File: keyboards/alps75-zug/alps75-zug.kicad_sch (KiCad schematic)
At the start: 176 parts, among them SW1 SW_Push, SW10 SW_Push, SW11 SW_Push, SW12 SW_Push, SW13 SW_Push, SW14 SW_Push, SW15 SW_Push, SW16 SW_Push, SW17 SW_Push, SW18 SW_Push, SW19 SW_Push, SW2 SW_Push, SW20 SW_Push, SW21 SW_Push, SW22 SW_Push, SW23 SW_Push, SW24 SW_Push, SW25 SW_Push, SW26 SW_Push, SW27 SW_Push, SW28 SW_Push, SW29 SW_Push, SW3 SW_Push, SW30 SW_Push, SW31 SW_Push, SW32 SW_Push, SW33 SW_Push, SW34 SW_Push, SW35 SW_Push, SW36 SW_Push, SW37 SW_Push, SW38 SW_Push, SW39 SW_Push, SW4 SW_Push, SW40 SW_Push, SW41 SW_Push, SW42 SW_Push, SW43 SW_Push, SW44 SW_Push, SW45 SW_Push, SW46 SW_Push, SW47 SW_Push, SW48 SW_Push, SW49 SW_Push, SW5 SW_Push, SW50 SW_Push, SW51 SW_Push, SW52 SW_Push, SW53 SW_Push, SW54 SW_Push, SW55 SW_Push, SW56 SW_Push, SW57 SW_Push, SW58 SW_Push, SW59 SW_Push, SW6 SW_Push, SW60 SW_Push, SW61 SW_Push, SW62 SW_Push, SW63 SW_Push, SW64 SW_Push, SW65 SW_Push, SW66 SW_Push, SW67 SW_Push, SW68 SW_Push, SW69 SW_Push, SW7 SW_Push, SW70 SW_Push, SW71 SW_Push, SW72 SW_Push, SW73 SW_Push, SW74 SW_Push, SW75 SW_Push, SW76 SW_Push, SW77 SW_Push, SW78 SW_Push, SW79 SW_Push, SW8 SW_Push, SW80 SW_Push, SW81 SW_Push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

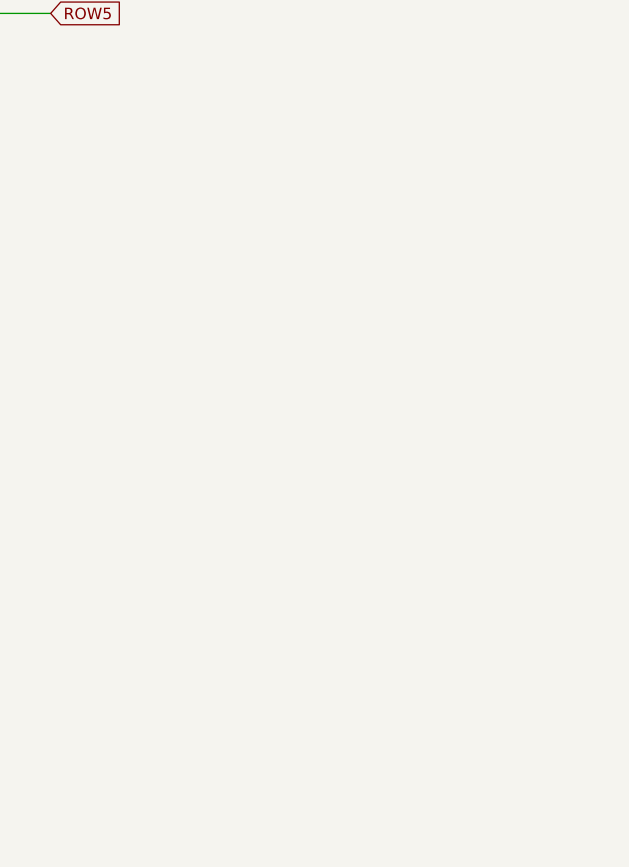
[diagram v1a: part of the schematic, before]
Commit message: Connected all diodes for F-keys + move COL14 wire out of way
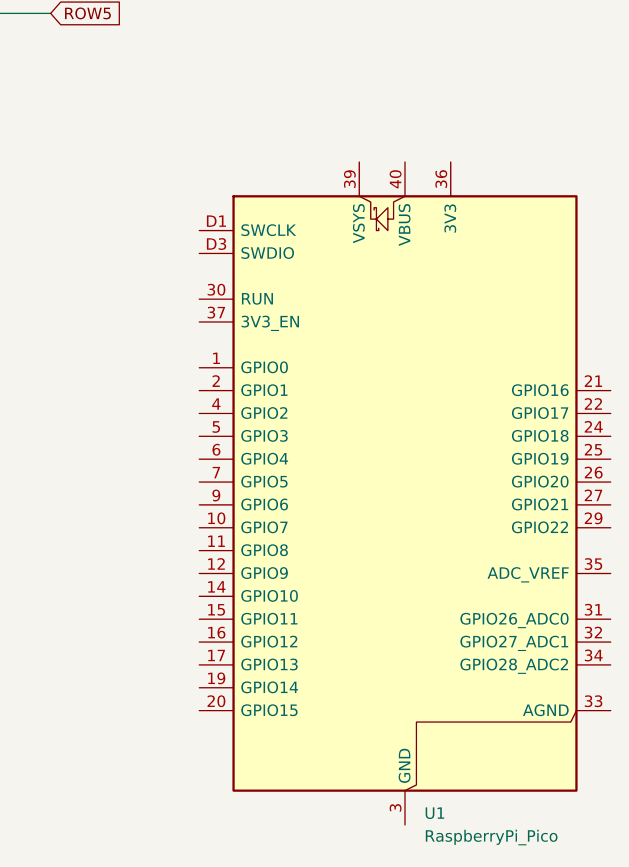
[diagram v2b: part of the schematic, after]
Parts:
- added U1: RaspberryPi_Pico, Module:RaspberryPi_Pico_SMD_HandSolder, symbol MCU_Module:RaspberryPi_Pico_Debug
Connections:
- new net: U1.13 (GND), U1.18 (GND), U1.23 (GND), U1.28 (GND), U1.3 (GND), U1.38 (GND), U1.8 (GND), U1.D2 (GND)
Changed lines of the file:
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@@
+	)
+	(symbol
+		(lib_id "MCU_Module:RaspberryPi_Pico_Debug")
+		(at 280.67 191.77 0)
+		(unit 1)
+		(body_style 1)
+		(exclude_from_sim no)
+		(in_bom yes)
+		(on_board yes)
+		(in_pos_files yes)
+		(dnp no)
+		(fields_autoplaced yes)
+		(property "Reference" "U1"
+			(at 282.8133 226.06 0)
+			(show_name no)
+			(do_not_autoplace no)
+			(effects
+				(font
+					(size 1.27 1.27)
+				)
+				(justify left)
+			)
+		)
+		(property "Value" "RaspberryPi_Pico"
+			(at 282.8133 228.6 0)
+			(show_name no)
+			(do_not_autoplace no)
+			(effects
+				(font
+					(size 1.27 1.27)
+				)
+				(justify left)
+			)
+		)
+		(property "Footprint" "Module:RaspberryPi_Pico_SMD_HandSolder"
+			(at 280.67 238.76 0)
+			(hide yes)
+			(show_name no)
+			(do_not_autoplace no)
+			(effects
+				(font
+					(size 1.27 1.27)
+				)
+			)
+		)
+		(property "Datasheet" "https://datasheets.raspberrypi.com/pico/pico-datasheet.pdf"
+			(at 280.67 241.3 0)
+			(hide yes)
+			(show_name no)
+			(do_not_autoplace no)
+			(effects
+				(font
+					(size 1.27 1.27)
+				)
+			)
+		)
+		(property "Description" "Versatile and inexpensive microcontroller module (with debug pins) powered by RP2040 dual-core Arm Cortex-M0+ processor up to 133 MHz, 264kB SRAM, 2MB QSPI flash; also supports Raspberry Pi Pico 2"
+			(at 280.67 243.84 0)
+			(hide yes)
+			(show_name no)
+			(do_not_autoplace no)
+			(effects
+				(font
+					(size 1.27 1.27)
+				)
+			)
+		)
+		(pin "25"
+		)
+		(pin "26"
+		)
+		(pin "24"
+		)
+		(pin "27"
+		)
+		(pin "22"
+		)
+		(pin "23"
+		)
+		(pin "5"
+		)
+		(pin "21"
+		)
+		(pin "20"
+		)
+		(pin "19"
+		)
+		(pin "18"
+		)
+		(pin "17"
+		)
+		(pin "16"
+		)
+		(pin "15"
+		)
+		(pin "14"
+		)
+		(pin "13"
+		)
+		(pin "12"
+		)
+		(pin "11"
+		)
+		(pin "9"
+		)
+		(pin "10"
+		)
+		(pin "7"
+		)
+		(pin "8"
+		)
+		(pin "6"
+		)
+		(pin "1"
+		)
+		(pin "2"
+		)
+		(pin "3"
+		)
+		(pin "4"
+		)
+		(pin "D3"
+		)
+		(pin "29"
+		)
+		(pin "30"
+		)
+		(pin "31"
+		)
+		(pin "32"
+		)
+		(pin "33"
+		)
+		(pin "34"
+		)
+		(pin "35"
+		)
+		(pin "28"
+		)
+		(pin "36"
+		)
+		(pin "D2"
+		)
+		(pin "D1"
+		)
+		(pin "40"
+		)
+		(pin "39"
+		)
+		(pin "38"
+		)
+		(pin "37"
+		)
+		(instances
+			(project "alps75-zug"
+				(path "/52ee5249-2c64-4583-bfc6-5b6d91f4f70c"
+					(reference "U1")
+					(unit 1)
+				)
+			)
+		)
 	)
 	(symbol

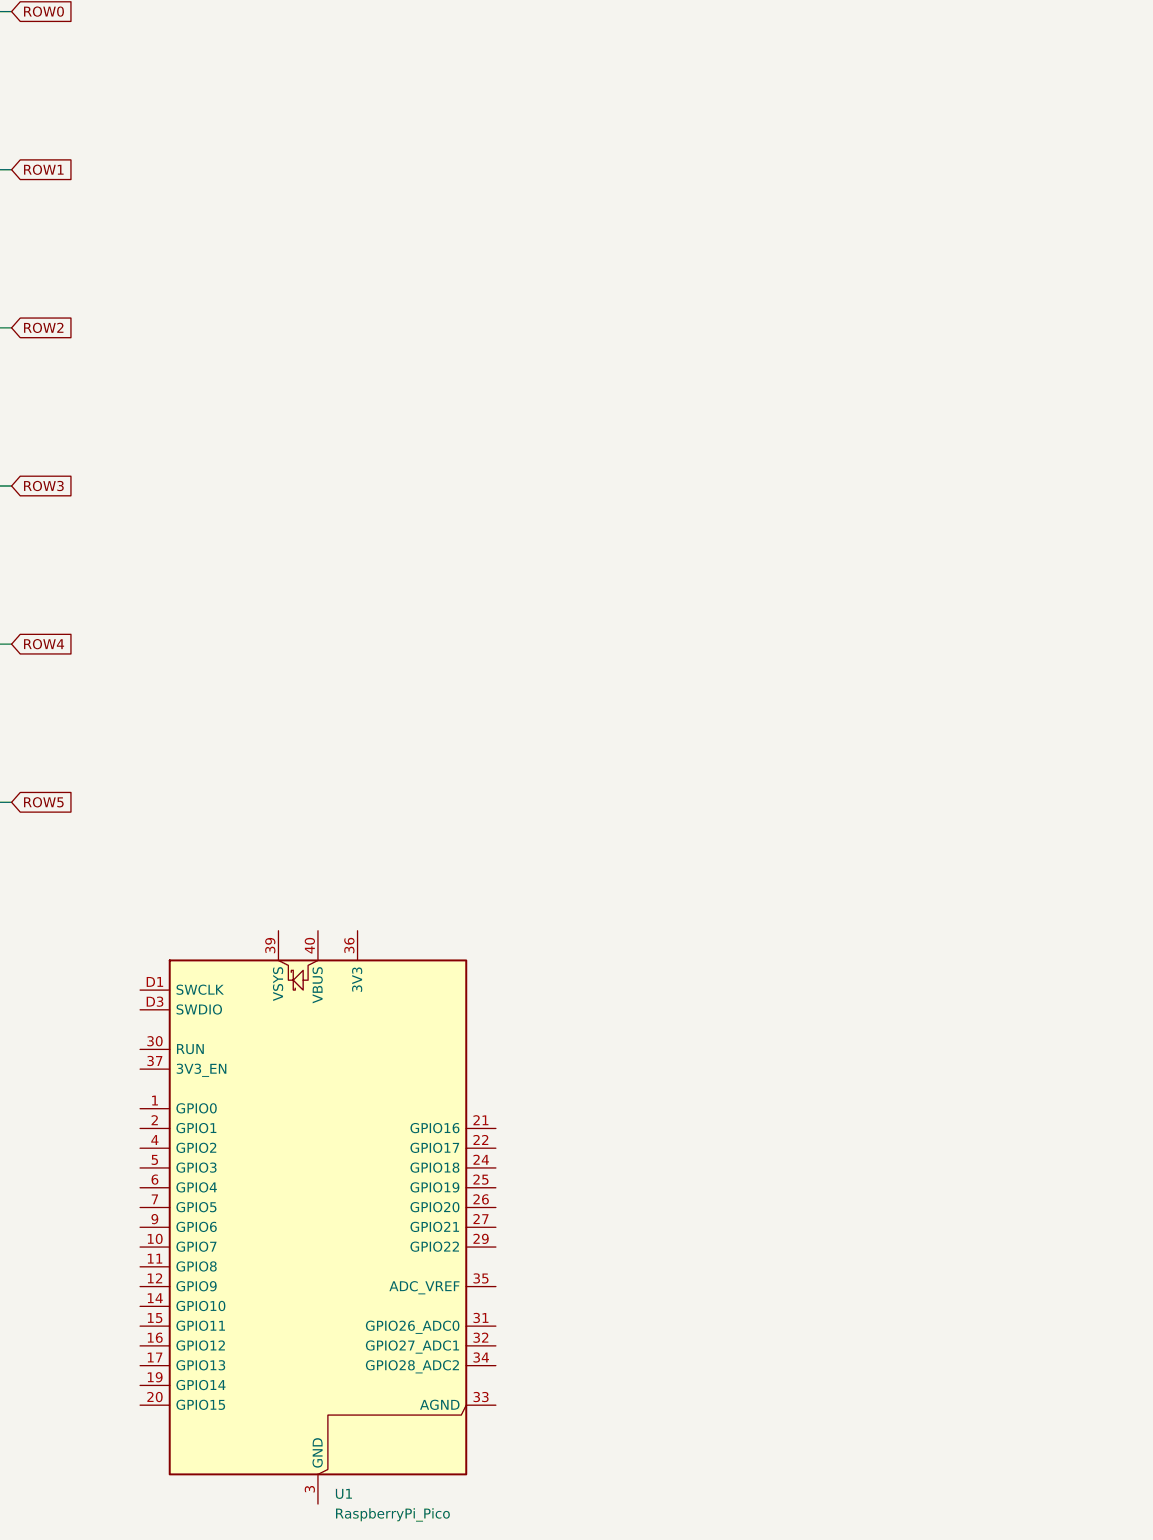
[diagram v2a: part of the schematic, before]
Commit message: Wire switches to MCU
PCB edges are updated to be the same on the side, cols wiring is from the F-key rows rather than from the bottom to shorten wiring, rows wiring from the right side of the PCB.
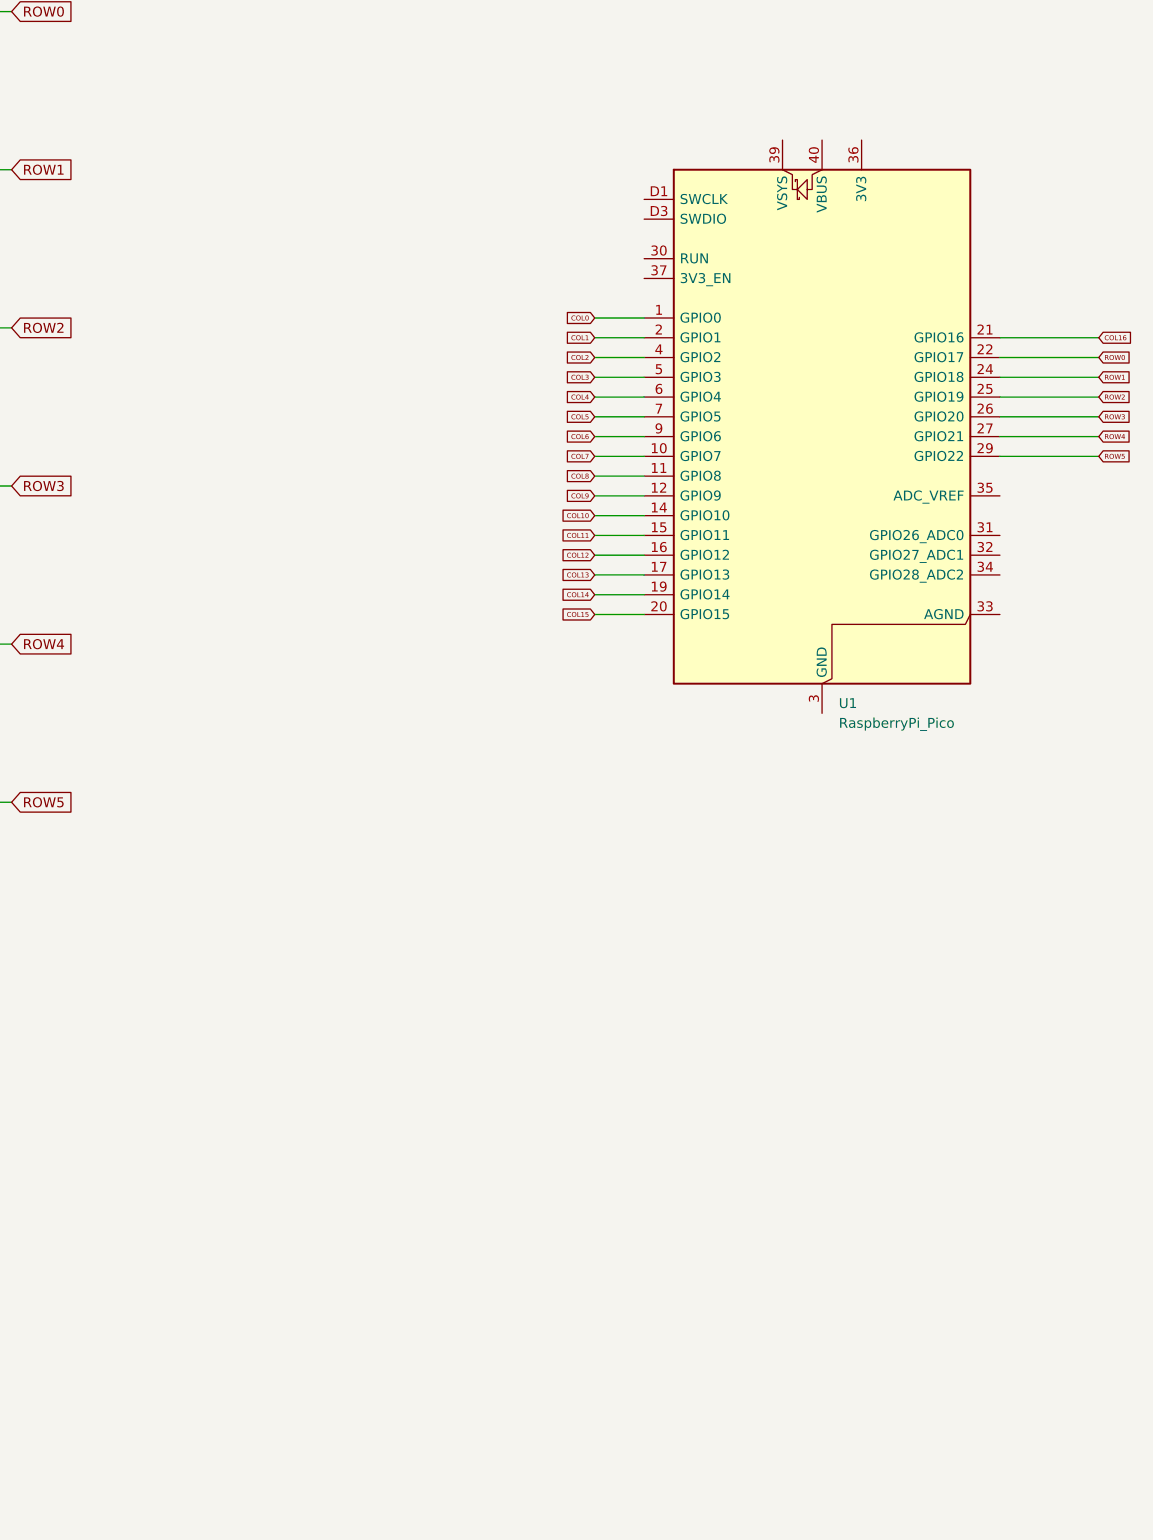
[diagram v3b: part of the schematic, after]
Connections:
- net COL0: now also U1.1 (GPIO0)
- net COL1: now also U1.2 (GPIO1)
- net COL10: now also U1.14 (GPIO10)
- net COL11: now also U1.15 (GPIO11)
- net COL12: now also U1.16 (GPIO12)
- net COL13: now also U1.17 (GPIO13)
- net COL14: now also U1.19 (GPIO14)
- net COL15: now also U1.20 (GPIO15)
- net COL16: now also U1.21 (GPIO16)
- net COL2: now also U1.4 (GPIO2)
- net COL3: now also U1.5 (GPIO3)
- net COL4: now also U1.6 (GPIO4)
- net COL5: now also U1.7 (GPIO5)
- net COL6: now also U1.9 (GPIO6)
- net COL7: now also U1.10 (GPIO7)
- net COL8: now also U1.11 (GPIO8)
- net COL9: now also U1.12 (GPIO9)
- net ROW0: now also U1.22 (GPIO17)
- net ROW1: now also U1.24 (GPIO18)
- net ROW2: now also U1.25 (GPIO19)
- net ROW3: now also U1.26 (GPIO20)
- net ROW4: now also U1.27 (GPIO21)
- net ROW5: now also U1.29 (GPIO22)
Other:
- moved on the sheet: U1
